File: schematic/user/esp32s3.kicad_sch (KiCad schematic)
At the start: 9 parts, among them SW1 ESP32S3 Reset, SW2 ESP32S3 Boot Method, U5 ESP32-S3-WROOM-1-N16R8

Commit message: v0.4 board: add MOSFET power control for TLV320 and other peripherals
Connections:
- net GPIO40_PERIPH_PWR: now reaches U5.33 (IO40)
- no-connect marks 13 -> 12
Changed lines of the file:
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@@
   )
   (no_connect (at 187.96 125.73))
-  (no_connect (at 187.96 110.49))
   (no_connect (at 187.96 107.95))
   (no_connect (at 187.96 105.41))
@@
     (stroke (width 0) (type default) (color 0 0 0 0))
   )
+  (wire (pts (xy 187.96 110.49) (xy 194.31 110.49))
+    (stroke (width 0) (type default) (color 0 0 0 0))
+  )
   (wire (pts (xy 151.13 107.95) (xy 157.48 107.95))
     (stroke (width 0) (type default) (color 0 0 0 0))
@@
     )
   )
+  (global_label "GPIO40_PERIPH_PWR" (shape input) (at 194.31 110.49 0) (fields_autoplaced)
+    (effects (font (size 1.27 1.27)) (justify left))
+    (property "Intersheet References" "${INTERSHEET_REFS}" (id 0) (at 216.4383 110.4106 0)
+      (effects (font (size 1.27 1.27)) (justify left) hide)
+    )
+  )

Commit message: v0.4 board: add thermistors for battery safety
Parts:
- added R35: 10K, Resistor_SMD:R_0402_1005Metric, symbol Device:R
- added TH2: SDNT2012X103F3950FTF, Resistor_SMD:R_0805_2012Metric, symbol Device:Thermistor_NTC
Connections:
- net GND: now also TH2.2
- net GPIO25_BOARD_TEMP: now reaches U5.25 (IO48)
- net GPIO25_BOARD_TEMP: now also R35.2, TH2.1
- new net 3.3V_PERIPH: R35.1
- no-connect marks 12 -> 11
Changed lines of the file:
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@@
   (junction (at 207.01 33.02) (diameter 0) (color 0 0 0 0)
   )
-  (no_connect (at 187.96 125.73))
+  (junction (at 124.46 163.83) (diameter 0) (color 0 0 0 0)
+  )
+  (no_connect (at 157.48 123.19))
   (no_connect (at 187.96 107.95))
   (no_connect (at 187.96 105.41))
   (no_connect (at 157.48 77.47))
   (no_connect (at 157.48 80.01))
-  (no_connect (at 157.48 123.19))
   (no_connect (at 157.48 125.73))
   (no_connect (at 187.96 102.87))
@@
     (stroke (width 0) (type default) (color 0 0 0 0))
   )
+  (wire (pts (xy 124.46 163.83) (xy 124.46 165.1))
+    (stroke (width 0) (type default) (color 0 0 0 0))
+  )
   (wire (pts (xy 151.13 118.11) (xy 157.48 118.11))
     (stroke (width 0) (type default) (color 0 0 0 0))
@@
     (stroke (width 0) (type default) (color 0 0 0 0))
   )
+  (wire (pts (xy 124.46 162.56) (xy 124.46 163.83))
+    (stroke (width 0) (type default) (color 0 0 0 0))
+  )
   (wire (pts (xy 67.31 107.95) (xy 72.39 107.95))
     (stroke (width 0) (type default) (color 0 0 0 0))
@@
     (stroke (width 0) (type default) (color 0 0 0 0))
   )
+  (wire (pts (xy 124.46 152.4) (xy 124.46 154.94))
+    (stroke (width 0) (type default) (color 0 0 0 0))
+  )
+  (wire (pts (xy 187.96 125.73) (xy 194.31 125.73))
+    (stroke (width 0) (type default) (color 0 0 0 0))
+  )
   (wire (pts (xy 201.93 40.64) (xy 201.93 44.45))
     (stroke (width 0) (type default) (color 0 0 0 0))
@@
     (stroke (width 0) (type default) (color 0 0 0 0))
   )
+  (wire (pts (xy 124.46 163.83) (xy 127 163.83))
+    (stroke (width 0) (type default) (color 0 0 0 0))
+  )
   (wire (pts (xy 201.93 33.02) (xy 187.96 33.02))
     (stroke (width 0) (type default) (color 0 0 0 0))
@@
     (stroke (width 0) (type default) (color 0 0 0 0))
   )
+  (wire (pts (xy 124.46 172.72) (xy 124.46 175.26))
+    (stroke (width 0) (type default) (color 0 0 0 0))
+  )
   (wire (pts (xy 86.36 58.42) (xy 86.36 60.96))
     (stroke (width 0) (type default) (color 0 0 0 0))
@@
     )
   )
+  (global_label "GPIO25_BOARD_TEMP" (shape input) (at 127 163.83 0) (fields_autoplaced)
+    (effects (font (size 1.27 1.27)) (justify left))
+    (property "Intersheet References" "${INTERSHEET_REFS}" (id 0) (at 149.3098 163.7506 0)
+      (effects (font (size 1.27 1.27)) (justify left) hide)
+    )
+  )
   (global_label "GPIO12_TLV320_MFP4" (shape input) (at 151.13 115.57 180) (fields_autoplaced)
     (effects (font (size 1.27 1.27)) (justify right))
@@
     )
   )
+  (global_label "3.3V_PERIPH" (shape output) (at 124.46 152.4 90) (fields_autoplaced)
+    (effects (font (size 1.27 1.27)) (justify left))
+    (property "Intersheet References" "${INTERSHEET_REFS}" (id 0) (at 124.3806 138.0126 90)
+      (effects (font (size 1.27 1.27)) (justify left) hide)
+    )
+  )
   (global_label "GPIO13_TLV320_RESET" (shape input) (at 151.13 118.11 180) (fields_autoplaced)
     (effects (font (size 1.27 1.27)) (justify right))
@@
     (property "Intersheet References" "${INTERSHEET_REFS}" (id 0) (at -152.4 85.09 0)
       (effects (font (size 1.27 1.27)) hide)
+    )
+  )
+  (global_label "GPIO25_BOARD_TEMP" (shape output) (at 194.31 125.73 0) (fields_autoplaced)
+    (effects (font (size 1.27 1.27)) (justify left))
+    (property "Intersheet References" "${INTERSHEET_REFS}" (id 0) (at 216.6198 125.8094 0)
+      (effects (font (size 1.27 1.27)) (justify left) hide)
     )
   )
@@
     )
     (property "LCSC" "C99782" (id 4) (at 71.12 143.51 0)
+      (effects (font (size 1.27 1.27)) hide)
+    )
+    (pin "1")
+    (pin "2")
+  )
+  (symbol (lib_id "Device:R") (at 124.46 158.75 0) (unit 1)
+    (in_bom yes) (on_board yes) (fields_autoplaced)
+    (property "Reference" "R35" (id 0) (at 126.238 157.9153 0)
+      (effects (font (size 1.27 1.27)) (justify left))
+    )
+    (property "Value" "10K" (id 1) (at 126.238 160.4522 0)
+      (effects (font (size 1.27 1.27)) (justify left))
+    )
+    (property "Footprint" "Resistor_SMD:R_0402_1005Metric" (id 2) (at 122.682 158.75 90)
+      (effects (font (size 1.27 1.27)) hide)
+    )
+    (property "Datasheet" "https://datasheet.lcsc.com/lcsc/2206010100_UNI-ROYAL-Uniroyal-Elec-0402WGF1002TCE_C25744.pdf" (id 3) (at 124.46 158.75 0)
+      (effects (font (size 1.27 1.27)) hide)
+    )
+    (property "LCSC" "C25744" (id 4) (at 124.46 158.75 0)
       (effects (font (size 1.27 1.27)) hide)
     )
@@
       (effects (font (size 1.27 1.27)) hide)
     )
+    (pin "1")
+  )
+  (symbol (lib_id "Device:Thermistor_NTC") (at 124.46 168.91 0) (unit 1)
+    (in_bom yes) (on_board yes) (fields_autoplaced)
+    (property "Reference" "TH2" (id 0) (at 126.873 168.3928 0)
+      (effects (font (size 1.27 1.27)) (justify left))
+    )
+    (property "Value" "SDNT2012X103F3950FTF" (id 1) (at 126.873 170.9297 0)
+      (effects (font (size 1.27 1.27)) (justify left))
+    )
+    (property "Footprint" "Resistor_SMD:R_0805_2012Metric" (id 2) (at 124.46 167.64 0)
+      (effects (font (size 1.27 1.27)) hide)
+    )
+    (property "Datasheet" "https://datasheet.lcsc.com/lcsc/2110081230_Sunlord-SDNT2012X103F3950FTF_C95968.pdf" (id 3) (at 124.46 167.64 0)
+      (effects (font (size 1.27 1.27)) hide)
+    )
+    (property "LCSC" "C95968" (id 4) (at 124.46 168.91 0)
+      (effects (font (size 1.27 1.27)) hide)
+    )
+    (pin "1")
+    (pin "2")
+  )
+  (symbol (lib_id "power:GND") (at 124.46 175.26 0) (unit 1)
+    (in_bom yes) (on_board yes) (fields_autoplaced)
+    (property "Reference" "#PWR04" (id 0) (at 124.46 181.61 0)
+      (effects (font (size 1.27 1.27)) hide)
+    )
+    (property "Value" "GND" (id 1) (at 124.46 179.7034 0))
+    (property "Footprint" "" (id 2) (at 124.46 175.26 0)
+      (effects (font (size 1.27 1.27)) hide)
+    )
+    (property "Datasheet" "" (id 3) (at 124.46 175.26 0)
+      (effects (font (size 1.27 1.27)) hide)
+    )

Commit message: v0.4 board submitted for build/assembly.
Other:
- company: (none) -> FreeDV Project
- title: (none) -> ezDV ESP32-S3
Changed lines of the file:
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@@
 (kicad_sch (version 20211123) (generator eeschema)
   (paper "A4")
+  (title_block
+    (title "ezDV ESP32-S3")
+    (date "2022-10-01")
+    (rev "v0.4")
+    (company "FreeDV Project")
+  )
   (junction (at 74.93 139.7) (diameter 0) (color 0 0 0 0)
   )

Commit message: v0.5 board: reroute temp sensor ADC to GPIO 18.
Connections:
- net GPIO18_BOARD_TEMP: now reaches U5.11 (IO18)
- net GPIO18_BOARD_TEMP: now also R35.2, TH2.1
- removed net GPIO25_BOARD_TEMP: R35.2, TH2.1, U5.25 (IO48)
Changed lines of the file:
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@@
   (junction (at 124.46 163.83) (diameter 0) (color 0 0 0 0)
   )
+  (no_connect (at 187.96 125.73))
   (no_connect (at 157.48 123.19))
   (no_connect (at 187.96 107.95))
@@
   (no_connect (at 187.96 100.33))
   (no_connect (at 187.96 97.79))
-  (no_connect (at 187.96 87.63))
   (no_connect (at 187.96 85.09))
   (wire (pts (xy 187.96 118.11) (xy 194.31 118.11))
@@
     (stroke (width 0) (type default) (color 0 0 0 0))
   )
+  (wire (pts (xy 187.96 87.63) (xy 194.31 87.63))
+    (stroke (width 0) (type default) (color 0 0 0 0))
+  )
   (wire (pts (xy 151.13 102.87) (xy 157.48 102.87))
     (stroke (width 0) (type default) (color 0 0 0 0))
@@
     (stroke (width 0) (type default) (color 0 0 0 0))
   )
-  (wire (pts (xy 187.96 125.73) (xy 194.31 125.73))
-    (stroke (width 0) (type default) (color 0 0 0 0))
-  )
   (wire (pts (xy 201.93 40.64) (xy 201.93 44.45))
     (stroke (width 0) (type default) (color 0 0 0 0))
@@
     )
   )
-  (global_label "GPIO25_BOARD_TEMP" (shape input) (at 127 163.83 0) (fields_autoplaced)
+  (global_label "GPIO18_BOARD_TEMP" (shape input) (at 127 163.83 0) (fields_autoplaced)
     (effects (font (size 1.27 1.27)) (justify left))
     (property "Intersheet References" "${INTERSHEET_REFS}" (id 0) (at 149.3098 163.7506 0)
@@
     )
   )
-  (global_label "GPIO25_BOARD_TEMP" (shape output) (at 194.31 125.73 0) (fields_autoplaced)
-    (effects (font (size 1.27 1.27)) (justify left))
-    (property "Intersheet References" "${INTERSHEET_REFS}" (id 0) (at 216.6198 125.8094 0)
-      (effects (font (size 1.27 1.27)) (justify left) hide)
-    )
+  (global_label "GPIO18_BOARD_TEMP" (shape output) (at 194.31 87.63 0) (fields_autoplaced)
+    (effects (font (size 1.27 1.27)) (justify left))
+    (property "Intersheet References" "${INTERSHEET_REFS}" (id 0) (at 216.6198 87.5506 0)
+      (effects (font (size 1.27 1.27)) (justify left) hide)
+    )

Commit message: v0.5 board: add I2C breakout header for potential future OLED screen integration.
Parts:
- added J4: I2C Breakout, Connector_PinHeader_2.54mm:PinHeader_1x04_P2.54mm_Vertical, symbol Connector:Conn_01x04_Female
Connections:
- net 3.3V_PERIPH: now also J4.4 (Pin_4)
- net GND: now also J4.1 (Pin_1)
- net GPIO45_SCL: now also J4.3 (Pin_3)
- net GPIO47_SDA: now also J4.2 (Pin_2)
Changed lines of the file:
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@@
   (junction (at 95.25 107.95) (diameter 0) (color 0 0 0 0)
   )
+  (junction (at 71.12 149.86) (diameter 0) (color 0 0 0 0)
+  )
   (junction (at 86.36 58.42) (diameter 0) (color 0 0 0 0)
+  )
+  (junction (at 78.74 149.86) (diameter 0) (color 0 0 0 0)
   )
   (junction (at 207.01 44.45) (diameter 0) (color 0 0 0 0)
@@
     (stroke (width 0) (type default) (color 0 0 0 0))
   )
+  (wire (pts (xy 76.2 156.21) (xy 76.2 161.29))
+    (stroke (width 0) (type default) (color 0 0 0 0))
+  )
   (wire (pts (xy 124.46 163.83) (xy 124.46 165.1))
     (stroke (width 0) (type default) (color 0 0 0 0))
@@
     (stroke (width 0) (type default) (color 0 0 0 0))
   )
+  (wire (pts (xy 68.58 158.75) (xy 71.12 158.75))
+    (stroke (width 0) (type default) (color 0 0 0 0))
+  )
+  (wire (pts (xy 73.66 156.21) (xy 73.66 161.29))
+    (stroke (width 0) (type default) (color 0 0 0 0))
+  )
   (wire (pts (xy 71.12 147.32) (xy 71.12 149.86))
     (stroke (width 0) (type default) (color 0 0 0 0))
@@
     (stroke (width 0) (type default) (color 0 0 0 0))
   )
+  (wire (pts (xy 71.12 158.75) (xy 71.12 161.29))
+    (stroke (width 0) (type default) (color 0 0 0 0))
+  )
   (wire (pts (xy 151.13 90.17) (xy 157.48 90.17))
     (stroke (width 0) (type default) (color 0 0 0 0))
   )
+  (wire (pts (xy 78.74 158.75) (xy 81.28 158.75))
+    (stroke (width 0) (type default) (color 0 0 0 0))
+  )
   (wire (pts (xy 151.13 110.49) (xy 157.48 110.49))
     (stroke (width 0) (type default) (color 0 0 0 0))
@@
     (stroke (width 0) (type default) (color 0 0 0 0))
   )
+  (wire (pts (xy 71.12 156.21) (xy 73.66 156.21))
+    (stroke (width 0) (type default) (color 0 0 0 0))
+  )
   (wire (pts (xy 124.46 163.83) (xy 127 163.83))
     (stroke (width 0) (type default) (color 0 0 0 0))
   )
+  (wire (pts (xy 78.74 149.86) (xy 78.74 156.21))
+    (stroke (width 0) (type default) (color 0 0 0 0))
+  )
   (wire (pts (xy 201.93 33.02) (xy 187.96 33.02))
     (stroke (width 0) (type default) (color 0 0 0 0))
@@
     (stroke (width 0) (type default) (color 0 0 0 0))
   )
+  (wire (pts (xy 71.12 149.86) (xy 71.12 156.21))
+    (stroke (width 0) (type default) (color 0 0 0 0))
+  )
   (wire (pts (xy 151.13 97.79) (xy 157.48 97.79))
     (stroke (width 0) (type default) (color 0 0 0 0))
@@
     (stroke (width 0) (type default) (color 0 0 0 0))
   )
+  (wire (pts (xy 78.74 161.29) (xy 78.74 158.75))
+    (stroke (width 0) (type default) (color 0 0 0 0))
+  )
   (wire (pts (xy 151.13 120.65) (xy 157.48 120.65))
     (stroke (width 0) (type default) (color 0 0 0 0))
@@
     (stroke (width 0) (type default) (color 0 0 0 0))
   )
+  (wire (pts (xy 78.74 156.21) (xy 76.2 156.21))
+    (stroke (width 0) (type default) (color 0 0 0 0))
+  )
   (wire (pts (xy 74.93 139.7) (xy 71.12 139.7))
     (stroke (width 0) (type default) (color 0 0 0 0))
@@
   (wire (pts (xy 187.96 120.65) (xy 194.31 120.65))
     (stroke (width 0) (type default) (color 0 0 0 0))
+  )
+  (global_label "3.3V_PERIPH" (shape output) (at 68.58 158.75 180) (fields_autoplaced)
+    (effects (font (size 1.27 1.27)) (justify right))
+    (property "Intersheet References" "${INTERSHEET_REFS}" (id 0) (at 54.1926 158.8294 0)
+      (effects (font (size 1.27 1.27)) (justify right) hide)
+    )
   )
   (global_label "GPIO8_BAT_ALERT" (shape output) (at 151.13 105.41 180) (fields_autoplaced)
@@
     (pin "1")
     (pin "2")
+  )
+  (symbol (lib_id "Connector:Conn_01x04_Female") (at 76.2 166.37 270) (unit 1)
+    (in_bom yes) (on_board yes) (fields_autoplaced)
+    (property "Reference" "J4" (id 0) (at 74.93 168.3496 90))
+    (property "Value" "I2C Breakout" (id 1) (at 74.93 170.8865 90))
+    (property "Footprint" "Connector_PinHeader_2.54mm:PinHeader_1x04_P2.54mm_Vertical" (id 2) (at 76.2 166.37 0)
+      (effects (font (size 1.27 1.27)) hide)
+    )
+    (property "Datasheet" "~" (id 3) (at 76.2 166.37 0)
+      (effects (font (size 1.27 1.27)) hide)
+    )
+    (pin "1")
+    (pin "2")
+    (pin "3")
+    (pin "4")
   )
   (symbol (lib_id "Switch:SW_Push") (at 77.47 96.52 0) (unit 1)
@@
     (pin "2")
   )
+  (symbol (lib_id "power:GND") (at 81.28 158.75 90) (unit 1)
+    (in_bom yes) (on_board yes) (fields_autoplaced)
+    (property "Reference" "#PWR0103" (id 0) (at 87.63 158.75 0)
+      (effects (font (size 1.27 1.27)) hide)
+    )
+    (property "Value" "GND" (id 1) (at 84.455 159.1838 90)
+      (effects (font (size 1.27 1.27)) (justify right))
+    )
+    (property "Footprint" "" (id 2) (at 81.28 158.75 0)
+      (effects (font (size 1.27 1.27)) hide)
+    )
+    (property "Datasheet" "" (id 3) (at 81.28 158.75 0)
+      (effects (font (size 1.27 1.27)) hide)
+    )
+    (pin "1")
+  )
   (symbol (lib_id "Device:C") (at 201.93 36.83 0) (unit 1)

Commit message: v0.5 board: move PERIPH_PWR GPIO to RTC to make sure it stays off when sleeping.
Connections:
- net 3.3V: no longer R19.1, R20.1
- net 3.3V_PERIPH: now also R19.1, R20.1
- net GPIO17_PERIPH_PWR: now reaches U5.10 (IO17)
- net GPIO40_PERIPH_PWR: no longer names the net of U5.33 (IO40)
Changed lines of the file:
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@@
   (no_connect (at 157.48 80.01))
   (no_connect (at 157.48 125.73))
+  (no_connect (at 194.31 110.49))
   (no_connect (at 187.96 102.87))
   (no_connect (at 187.96 100.33))
   (no_connect (at 187.96 97.79))
-  (no_connect (at 187.96 85.09))
   (wire (pts (xy 187.96 118.11) (xy 194.31 118.11))
     (stroke (width 0) (type default) (color 0 0 0 0))
@@
     (stroke (width 0) (type default) (color 0 0 0 0))
   )
+  (wire (pts (xy 187.96 85.09) (xy 193.04 85.09))
+    (stroke (width 0) (type default) (color 0 0 0 0))
+  )
   (wire (pts (xy 187.96 120.65) (xy 194.31 120.65))
     (stroke (width 0) (type default) (color 0 0 0 0))
@@
     )
   )
-  (global_label "GPIO40_PERIPH_PWR" (shape input) (at 194.31 110.49 0) (fields_autoplaced)
-    (effects (font (size 1.27 1.27)) (justify left))
-    (property "Intersheet References" "${INTERSHEET_REFS}" (id 0) (at 216.4383 110.4106 0)
+  (global_label "GPIO17_PERIPH_PWR" (shape input) (at 193.04 85.09 0) (fields_autoplaced)
+    (effects (font (size 1.27 1.27)) (justify left))
+    (property "Intersheet References" "${INTERSHEET_REFS}" (id 0) (at 215.1683 85.0106 0)
       (effects (font (size 1.27 1.27)) (justify left) hide)
     )
@@
     )
   )
-  (global_label "3.3V" (shape output) (at 74.93 134.62 90) (fields_autoplaced)
-    (effects (font (size 1.27 1.27)) (justify left))
-    (property "Intersheet References" "${INTERSHEET_REFS}" (id 0) (at -152.4 85.09 0)
-      (effects (font (size 1.27 1.27)) hide)
-    )
-  )
+  (global_label "3.3V_PERIPH" (shape output) (at 74.93 134.62 90) (fields_autoplaced)
+    (effects (font (size 1.27 1.27)) (justify left))
+    (property "Intersheet References" "${INTERSHEET_REFS}" (id 0) (at 74.8506 120.2326 90)
+      (effects (font (size 1.27 1.27)) (justify left) hide)
+    )
+  )

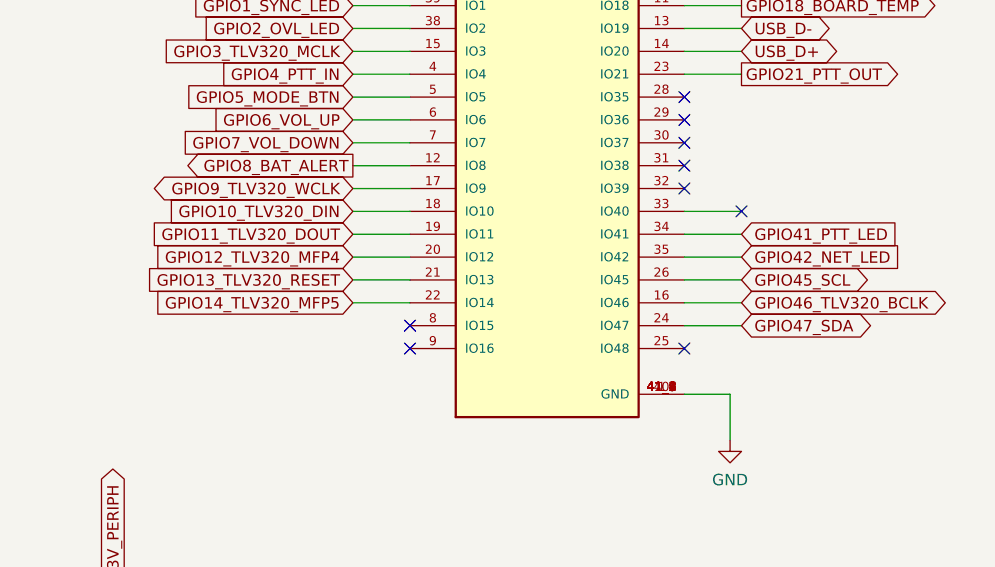
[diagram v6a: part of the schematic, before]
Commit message: v0.5 board: move PTT and NET GPIOs to RTC domain.
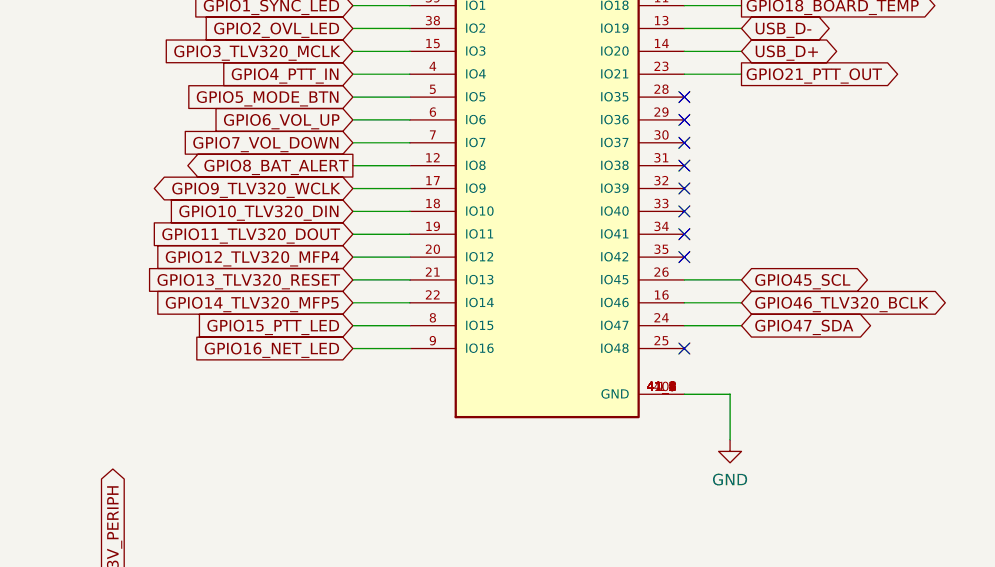
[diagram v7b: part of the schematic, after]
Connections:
- net GPIO15_PTT_LED: now reaches U5.8 (IO15)
- net GPIO16_NET_LED: now reaches U5.9 (IO16)
- net GPIO41_PTT_LED: no longer names the net of U5.34 (IO41)
- net GPIO42_NET_LED: no longer names the net of U5.35 (IO42)
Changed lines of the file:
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@@
   )
   (no_connect (at 187.96 125.73))
-  (no_connect (at 157.48 123.19))
   (no_connect (at 187.96 107.95))
   (no_connect (at 187.96 105.41))
   (no_connect (at 157.48 77.47))
   (no_connect (at 157.48 80.01))
-  (no_connect (at 157.48 125.73))
-  (no_connect (at 194.31 110.49))
+  (no_connect (at 187.96 110.49))
+  (no_connect (at 187.96 113.03))
+  (no_connect (at 187.96 115.57))
   (no_connect (at 187.96 102.87))
   (no_connect (at 187.96 100.33))
@@
     (stroke (width 0) (type default) (color 0 0 0 0))
   )
-  (wire (pts (xy 187.96 110.49) (xy 194.31 110.49))
-    (stroke (width 0) (type default) (color 0 0 0 0))
-  )
   (wire (pts (xy 151.13 107.95) (xy 157.48 107.95))
     (stroke (width 0) (type default) (color 0 0 0 0))
@@
     (stroke (width 0) (type default) (color 0 0 0 0))
   )
-  (wire (pts (xy 187.96 113.03) (xy 194.31 113.03))
-    (stroke (width 0) (type default) (color 0 0 0 0))
-  )
   (wire (pts (xy 187.96 123.19) (xy 194.31 123.19))
     (stroke (width 0) (type default) (color 0 0 0 0))
@@
     (stroke (width 0) (type default) (color 0 0 0 0))
   )
+  (wire (pts (xy 151.13 123.19) (xy 157.48 123.19))
+    (stroke (width 0) (type default) (color 0 0 0 0))
+  )
   (wire (pts (xy 71.12 147.32) (xy 71.12 149.86))
     (stroke (width 0) (type default) (color 0 0 0 0))
@@
     (stroke (width 0) (type default) (color 0 0 0 0))
   )
-  (wire (pts (xy 187.96 115.57) (xy 194.31 115.57))
-    (stroke (width 0) (type default) (color 0 0 0 0))
-  )
   (wire (pts (xy 187.96 95.25) (xy 194.31 95.25))
     (stroke (width 0) (type default) (color 0 0 0 0))
@@
     (stroke (width 0) (type default) (color 0 0 0 0))
   )
+  (wire (pts (xy 151.13 125.73) (xy 157.48 125.73))
+    (stroke (width 0) (type default) (color 0 0 0 0))
+  )
   (wire (pts (xy 78.74 161.29) (xy 78.74 158.75))
     (stroke (width 0) (type default) (color 0 0 0 0))
@@
     )
   )
-  (global_label "GPIO42_NET_LED" (shape input) (at 194.31 115.57 0) (fields_autoplaced)
-    (effects (font (size 1.27 1.27)) (justify left))
-    (property "Intersheet References" "${INTERSHEET_REFS}" (id 0) (at -66.04 78.74 0)
+  (global_label "GPIO16_NET_LED" (shape input) (at 151.13 125.73 180) (fields_autoplaced)
+    (effects (font (size 1.27 1.27)) (justify right))
+    (property "Intersheet References" "${INTERSHEET_REFS}" (id 0) (at 411.48 162.56 0)
       (effects (font (size 1.27 1.27)) hide)
     )
@@
     )
   )
-  (global_label "GPIO41_PTT_LED" (shape input) (at 194.31 113.03 0) (fields_autoplaced)
-    (effects (font (size 1.27 1.27)) (justify left))
-    (property "Intersheet References" "${INTERSHEET_REFS}" (id 0) (at -66.04 73.66 0)
-      (effects (font (size 1.27 1.27)) hide)
-    )
+  (global_label "GPIO15_PTT_LED" (shape input) (at 151.13 123.19 180) (fields_autoplaced)
+    (effects (font (size 1.27 1.27)) (justify right))
+    (property "Intersheet References" "${INTERSHEET_REFS}" (id 0) (at 411.48 162.56 0)
+      (effects (font (size 1.27 1.27)) hide)
+    )
